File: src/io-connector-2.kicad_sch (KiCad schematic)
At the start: 1 part

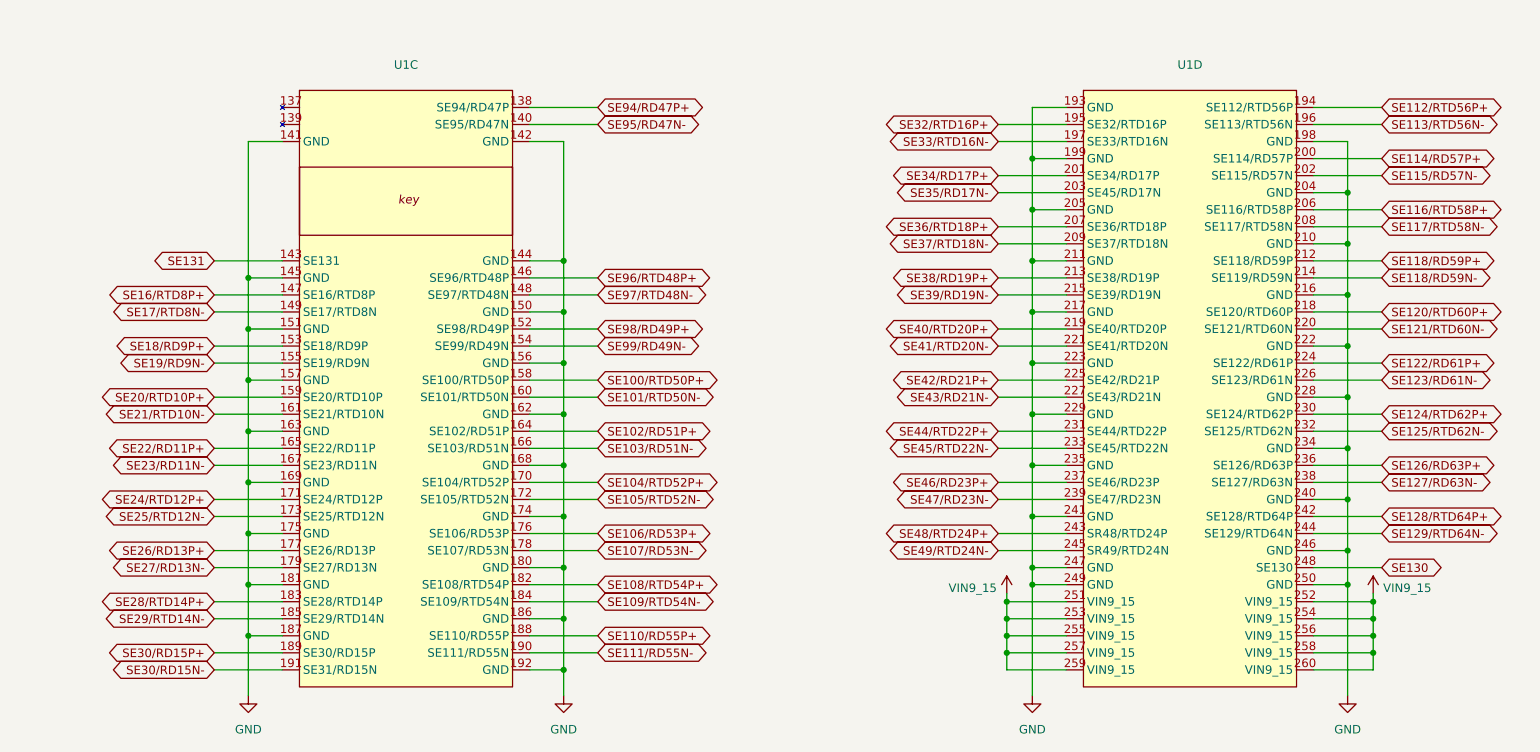
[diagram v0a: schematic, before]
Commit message: Updates the fpga configuration schematic
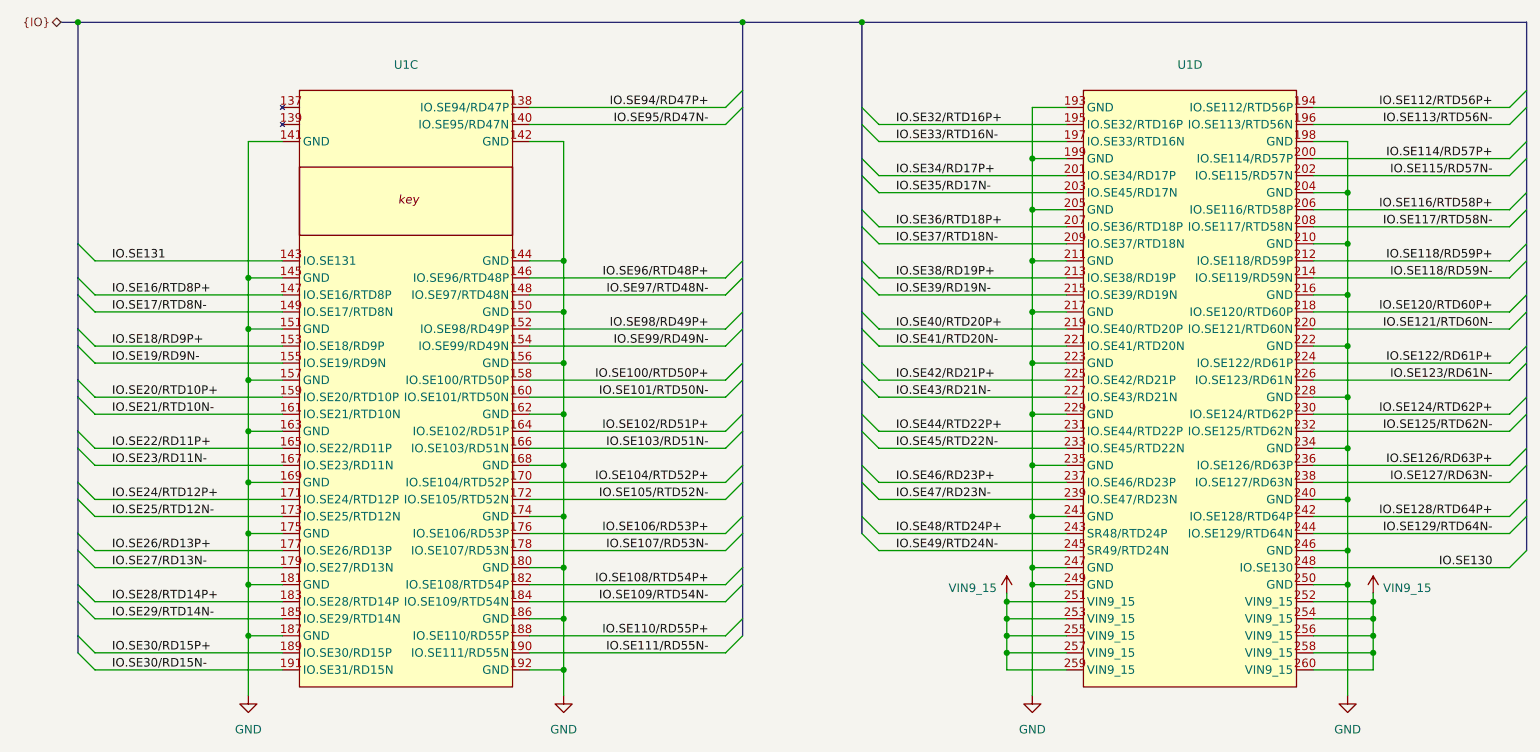
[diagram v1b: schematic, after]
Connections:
- net SE100/RTD50P+ renamed IO.SE100/RTD50P+
- net SE101/RTD50N- renamed IO.SE101/RTD50N-
- net SE102/RD51P+ renamed IO.SE102/RD51P+
- net SE103/RD51N- renamed IO.SE103/RD51N-
- net SE104/RTD52P+ renamed IO.SE104/RTD52P+
- net SE105/RTD52N- renamed IO.SE105/RTD52N-
- net SE106/RD53P+ renamed IO.SE106/RD53P+
- net SE107/RD53N- renamed IO.SE107/RD53N-
- net SE108/RTD54P+ renamed IO.SE108/RTD54P+
- net SE109/RTD54N- renamed IO.SE109/RTD54N-
- net SE110/RD55P+ renamed IO.SE110/RD55P+
- net SE111/RD55N- renamed IO.SE111/RD55N-
- net SE112/RTD56P+ renamed IO.SE112/RTD56P+
- net SE113/RTD56N- renamed IO.SE113/RTD56N-
- net SE114/RD57P+ renamed IO.SE114/RD57P+
- net SE115/RD57N- renamed IO.SE115/RD57N-
- net SE116/RTD58P+ renamed IO.SE116/RTD58P+
- net SE117/RTD58N- renamed IO.SE117/RTD58N-
- net SE118/RD59N- renamed IO.SE118/RD59N-
- net SE118/RD59P+ renamed IO.SE118/RD59P+
- net SE120/RTD60P+ renamed IO.SE120/RTD60P+
- net SE121/RTD60N- renamed IO.SE121/RTD60N-
- net SE122/RD61P+ renamed IO.SE122/RD61P+
- net SE123/RD61N- renamed IO.SE123/RD61N-
- net SE124/RTD62P+ renamed IO.SE124/RTD62P+
- net SE125/RTD62N- renamed IO.SE125/RTD62N-
- net SE126/RD63P+ renamed IO.SE126/RD63P+
- net SE127/RD63N- renamed IO.SE127/RD63N-
- net SE128/RTD64P+ renamed IO.SE128/RTD64P+
- net SE129/RTD64N- renamed IO.SE129/RTD64N-
- net SE130 renamed IO.SE130
- net SE131 renamed IO.SE131
- net SE16/RTD8P+ renamed IO.SE16/RTD8P+
- net SE17/RTD8N- renamed IO.SE17/RTD8N-
- net SE18/RD9P+ renamed IO.SE18/RD9P+
- net SE19/RD9N- renamed IO.SE19/RD9N-
- net SE20/RTD10P+ renamed IO.SE20/RTD10P+
- net SE21/RTD10N- renamed IO.SE21/RTD10N-
- net SE22/RD11P+ renamed IO.SE22/RD11P+
- net SE23/RD11N- renamed IO.SE23/RD11N-
- net SE24/RTD12P+ renamed IO.SE24/RTD12P+
- net SE25/RTD12N- renamed IO.SE25/RTD12N-
- net SE26/RD13P+ renamed IO.SE26/RD13P+
- net SE27/RD13N- renamed IO.SE27/RD13N-
- net SE28/RTD14P+ renamed IO.SE28/RTD14P+
- net SE29/RTD14N- renamed IO.SE29/RTD14N-
- net SE30/RD15N- renamed IO.SE30/RD15N-
- net SE30/RD15P+ renamed IO.SE30/RD15P+
- net SE32/RTD16P+ renamed IO.SE32/RTD16P+
- net SE33/RTD16N- renamed IO.SE33/RTD16N-
- net SE34/RD17P+ renamed IO.SE34/RD17P+
- net SE35/RD17N- renamed IO.SE35/RD17N-
- net SE36/RTD18P+ renamed IO.SE36/RTD18P+
- net SE37/RTD18N- renamed IO.SE37/RTD18N-
- net SE38/RD19P+ renamed IO.SE38/RD19P+
- net SE39/RD19N- renamed IO.SE39/RD19N-
- net SE40/RTD20P+ renamed IO.SE40/RTD20P+
- net SE41/RTD20N- renamed IO.SE41/RTD20N-
- net SE42/RD21P+ renamed IO.SE42/RD21P+
- net SE43/RD21N- renamed IO.SE43/RD21N-
- net SE44/RTD22P+ renamed IO.SE44/RTD22P+
- net SE45/RTD22N- renamed IO.SE45/RTD22N-
- net SE46/RD23P+ renamed IO.SE46/RD23P+
- net SE47/RD23N- renamed IO.SE47/RD23N-
- net SE48/RTD24P+ renamed IO.SE48/RTD24P+
- net SE49/RTD24N- renamed IO.SE49/RTD24N-
- net SE94/RD47P+ renamed IO.SE94/RD47P+
- net SE95/RD47N- renamed IO.SE95/RD47N-
- net SE96/RTD48P+ renamed IO.SE96/RTD48P+
- net SE97/RTD48N- renamed IO.SE97/RTD48N-
- net SE98/RD49P+ renamed IO.SE98/RD49P+
- net SE99/RD49N- renamed IO.SE99/RD49N-
